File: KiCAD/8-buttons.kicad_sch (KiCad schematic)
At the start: 3 parts, among them U1 74HC165, U2 TLC5917QDRQ1

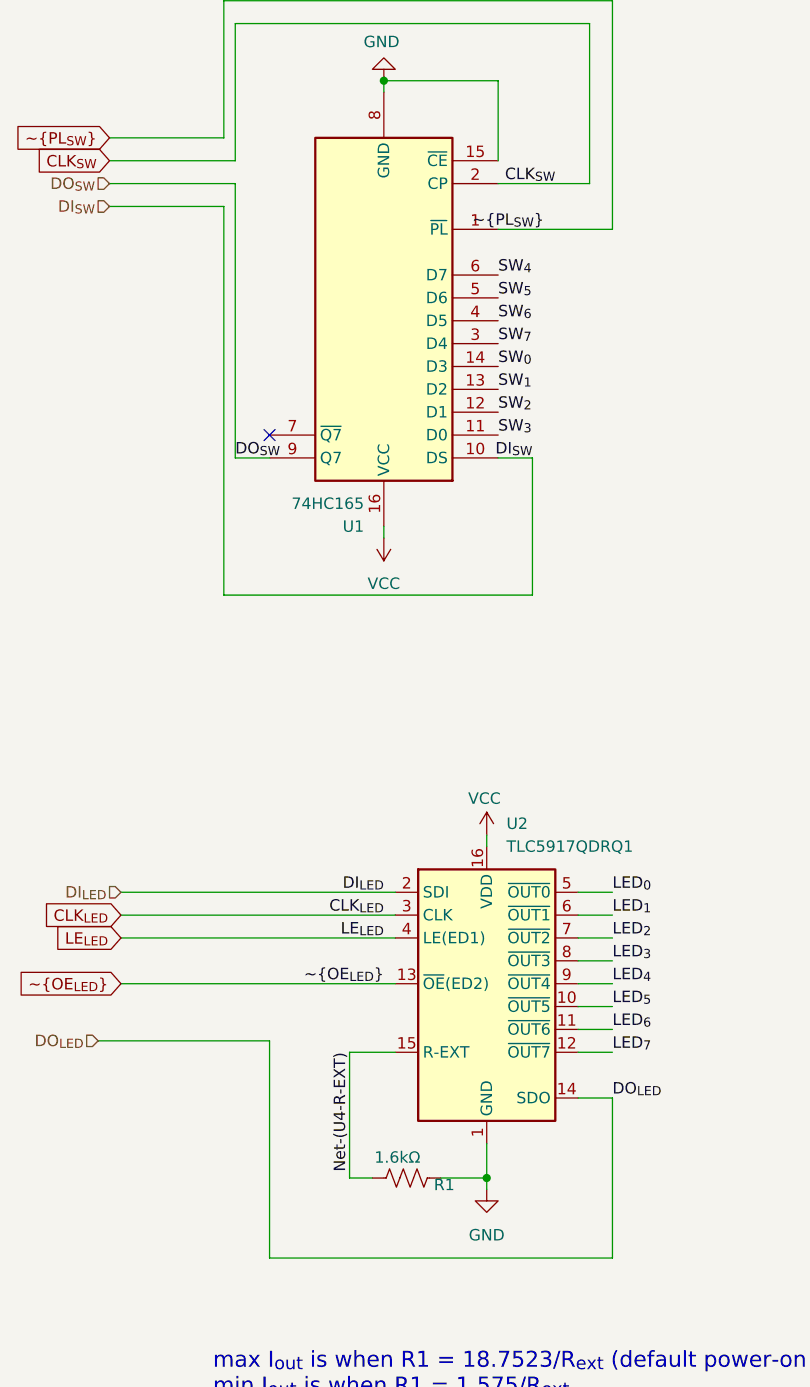
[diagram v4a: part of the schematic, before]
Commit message: fix ERC/DRC violations
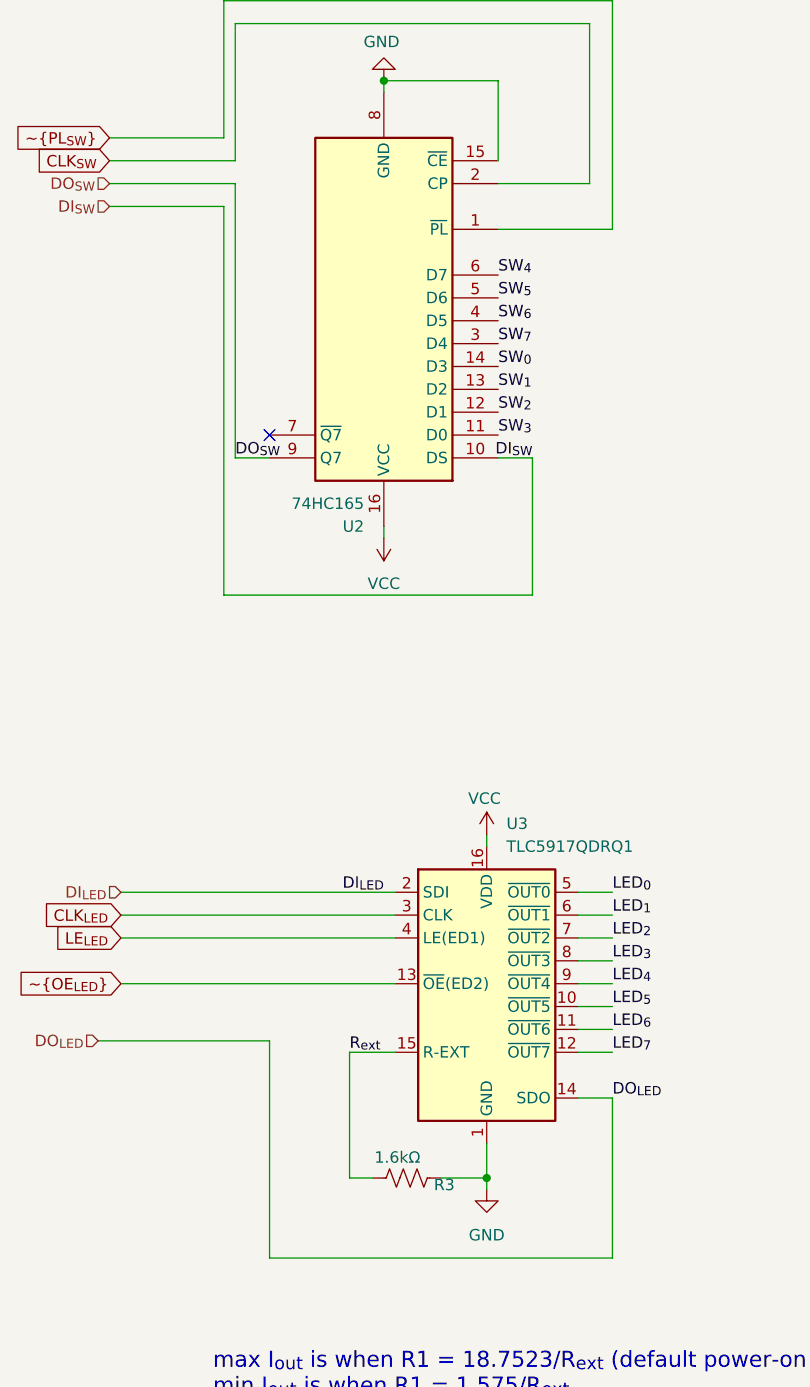
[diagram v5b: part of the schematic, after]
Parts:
- renumbered R1 to R3, U1 to U2, U2 to U3
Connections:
- net Net-(U4-R-EXT) renamed R_{ext}
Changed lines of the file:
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@@
+		)
+	)
+	(label "R_{ext}"
+		(at 54.61 139.7 0)
+		(effects
+			(font
+				(size 1.27 1.27)
+			)
+			(justify left bottom)
 		)
 	)
@@
 		)
 	)
-	(label "~{OE_{LED}}"
-		(at 58.42 132.08 180)
-		(effects
-			(font
-				(size 1.27 1.27)
-			)
-			(justify right bottom)
-		)
-	)
 	(label "SW_{2}"
 		(at 180.34 78.74 180)
@@
 		)
 	)
-	(label "LE_{LED}"
-		(at 58.42 127 180)
-		(effects
-			(font
-				(size 1.27 1.27)
-			)
-			(justify right bottom)
-		)
-	)
 	(label "LED_{1}"
 		(at 151.13 83.82 180)
@@
 		)
 	)
-	(label "CLK_{SW}"
-		(at 77.47 43.18 180)
-		(effects
-			(font
-				(size 1.27 1.27)
-			)
-			(justify right bottom)
-		)
-	)
-	(label "CLK_{LED}"
-		(at 58.42 124.46 180)
-		(effects
-			(font
-				(size 1.27 1.27)
-			)
-			(justify right bottom)
-		)
-	)
 	(label "SW_{0}"
 		(at 123.19 78.74 180)
@@
 		)
 	)
-	(label "Net-(U4-R-EXT)"
-		(at 54.61 139.7 270)
-		(effects
-			(font
-				(size 1.27 1.27)
-			)
-			(justify right bottom)
-		)
-	)
 	(label "LED_{4}"
 		(at 123.19 105.41 180)
@@
 	(label "SW_{4}"
 		(at 123.19 100.33 180)
-		(effects
-			(font
-				(size 1.27 1.27)
-			)
-			(justify right bottom)
-		)
-	)
-	(label "~{PL_{SW}}"
-		(at 76.2 48.26 180)
 		(effects
 			(font
@@
 		(dnp no)
 		(fields_autoplaced yes)
-		(property "Reference" "U2"
+		(property "Reference" "U3"
 			(at 72.0441 114.3 0)
 			(effects
@@
 			(project "DrumKitButtons"
 				(path "/9053e4fd-2214-4e2c-a1c2-d5a9964413b7/26123988-4436-470f-8df2-915b04ee2818"
+					(reference "U10")
+					(unit 1)
+				)
+				(path "/9053e4fd-2214-4e2c-a1c2-d5a9964413b7/56600e35-72e7-45c1-8008-a2a2285948a1"
+					(reference "U3")
+					(unit 1)
+				)
+				(path "/9053e4fd-2214-4e2c-a1c2-d5a9964413b7/575be80e-352b-49ee-9f93-701667605cc7"
+					(reference "U1")
+					(unit 1)
+				)
+				(path "/9053e4fd-2214-4e2c-a1c2-d5a9964413b7/750b8000-0e2b-48b2-9b84-94fc6d0905e1"
+					(reference "U5")
+					(unit 1)
+				)
+				(path "/9053e4fd-2214-4e2c-a1c2-d5a9964413b7/8e3d7c7f-97b6-485f-a62d-91a5d64f0541"
+					(reference "U8")
+					(unit 1)
+				)
+				(path "/9053e4fd-2214-4e2c-a1c2-d5a9964413b7/903f5d09-4594-4373-9fb5-e09f9cdba84a"
 					(reference "U11")
-					(unit 1)
-				)
-				(path "/9053e4fd-2214-4e2c-a1c2-d5a9964413b7/56600e35-72e7-45c1-8008-a2a2285948a1"
-					(reference "U2")
-					(unit 1)
-				)
-				(path "/9053e4fd-2214-4e2c-a1c2-d5a9964413b7/575be80e-352b-49ee-9f93-701667605cc7"
-					(reference "U4")
-					(unit 1)
-				)
-				(path "/9053e4fd-2214-4e2c-a1c2-d5a9964413b7/750b8000-0e2b-48b2-9b84-94fc6d0905e1"
-					(reference "U8")
-					(unit 1)
-				)
-				(path "/9053e4fd-2214-4e2c-a1c2-d5a9964413b7/8e3d7c7f-97b6-485f-a62d-91a5d64f0541"
-					(reference "U7")
-					(unit 1)
-				)
-				(path "/9053e4fd-2214-4e2c-a1c2-d5a9964413b7/903f5d09-4594-4373-9fb5-e09f9cdba84a"
-					(reference "U12")
 					(unit 1)
 				)
@@
 		(on_board yes)
 		(dnp no)
-		(property "Reference" "R1"
+		(property "Reference" "R3"
 			(at 66.294 154.432 90)
 			(effects
@@
 				)
 				(path "/9053e4fd-2214-4e2c-a1c2-d5a9964413b7/56600e35-72e7-45c1-8008-a2a2285948a1"
+					(reference "R3")
+					(unit 1)
+				)
+				(path "/9053e4fd-2214-4e2c-a1c2-d5a9964413b7/575be80e-352b-49ee-9f93-701667605cc7"
 					(reference "R1")
 					(unit 1)
 				)
-				(path "/9053e4fd-2214-4e2c-a1c2-d5a9964413b7/575be80e-352b-49ee-9f93-701667605cc7"
-					(reference "R2")
-					(unit 1)
-				)
 				(path "/9053e4fd-2214-4e2c-a1c2-d5a9964413b7/750b8000-0e2b-48b2-9b84-94fc6d0905e1"
-					(reference "R20")
+					(reference "R18")
 					(unit 1)
 				)
@@
 				)
 				(path "/9053e4fd-2214-4e2c-a1c2-d5a9964413b7/903f5d09-4594-4373-9fb5-e09f9cdba84a"
-					(reference "R38")
+					(reference "R36")
 					(unit 1)
 				)
@@
 		(dnp no)
 		(fields_autoplaced yes)
-		(property "Reference" "U1"
+		(property "Reference" "U2"
 			(at 56.2259 81.28 0)
 			(effects
@@
 				)
 				(path "/9053e4fd-2214-4e2c-a1c2-d5a9964413b7/56600e35-72e7-45c1-8008-a2a2285948a1"
-					(reference "U1")
+					(reference "U2")
 					(unit 1)
 				)
 				(path "/9053e4fd-2214-4e2c-a1c2-d5a9964413b7/575be80e-352b-49ee-9f93-701667605cc7"
-					(reference "U3")
+					(reference "U4")
 					(unit 1)
 				)
@@
 				)
 				(path "/9053e4fd-2214-4e2c-a1c2-d5a9964413b7/8e3d7c7f-97b6-485f-a62d-91a5d64f0541"
-					(reference "U5")
+					(reference "U7")
 					(unit 1)
 				)
 				(path "/9053e4fd-2214-4e2c-a1c2-d5a9964413b7/903f5d09-4594-4373-9fb5-e09f9cdba84a"
-					(reference "U10")
-					(unit 1)
-				)
+					(reference "U12")
+					(unit 1)
+				)
